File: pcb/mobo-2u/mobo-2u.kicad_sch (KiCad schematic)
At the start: 66 parts, among them J1 SWD_10, J2 PEEL_MOTOR, J3 DRIVE_MOTOR, J4 SW1, J5 SPRING_FINGERS, J6 SW2, J7 SW1, J8 USART1, J9 SWD_10, U1 STM32F031C6Tx, U2 STM32F031K6Ux, U4 AP1117-33, U5 MC34063AD, U6 MAX3078E, U7 DRV8837, U8 DRV8837, Y1 8MHz

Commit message: mega push, lots of cad updates, new pcb form factor and schematic rework
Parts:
- removed C12: 100uF, Capacitor_SMD:C_Elec_6.3x7.7, symbol Device:C_Polarized_Small
- removed C13, C9: 10u, Capacitor_SMD:C_0805_2012Metric, symbol Device:C_Small
- removed C14: 470pF, Capacitor_SMD:C_0805_2012Metric, symbol Device:C_Small
- removed C16: 470uF, Capacitor_SMD:C_Elec_6.3x7.7, symbol Device:C_Polarized_Small
- removed D1: LED_RGBA, index:MHS110FRGBCT, symbol Device:LED_RGBA
- removed D3: LED_RGBA_ALT, LED_SMD:LED_LiteOn_LTST-C19HE1WT, symbol Device:LED_RGBA
- removed D6: 1N5819, Diode_SMD:D_SOD-123, symbol Diode:1N5819
- removed J4, J7: SW1, feeder:1TS003B-1400-3500A-CT, symbol Connector:Conn_01x04_Female
- removed J6: SW2, feeder:1TS003B-1400-3500A-CT, symbol Connector:Conn_01x04_Female
- removed L1: 220uH, Inductor_SMD:L_6.3x6.3_H3, symbol pspice:INDUCTOR
- removed R2, R3, R5: 470, Resistor_SMD:R_0805_2012Metric, symbol Device:R_Small
- removed U1: STM32F031C6Tx, Package_QFP:LQFP-48_7x7mm_P0.5mm, symbol MCU_ST_STM32F0:STM32F031C6Tx
- removed U2: STM32F031K6Ux, Package_DFN_QFN:QFN-32-1EP_5x5mm_P0.5mm_EP3.45x3.45mm, symbol MCU_ST_STM32F0:STM32F031K6Ux
- removed U4: AP1117-33, Package_TO_SOT_SMD:SOT-223-3_TabPin2, symbol Regulator_Linear:AP1117-33
- removed U5: MC34063AD, Package_SO:SOIC-8_3.9x4.9mm_P1.27mm, symbol Regulator_Switching:MC34063AD
- added C15, C21, C25, C26, C27, C28: 10u, Capacitor_SMD:C_0805_2012Metric, symbol Device:C_Small
- added C16: 1u, Capacitor_SMD:C_0805_2012Metric, symbol Device:C_Small
- added C22: 4.7n, Capacitor_SMD:C_0805_2012Metric, symbol Device:C_Small
- added C23: 47p, Capacitor_SMD:C_0805_2012Metric, symbol Device:C_Small
- added C24: 100n, Capacitor_SMD:C_0805_2012Metric, symbol Device:C_Small
- added C29: 0.1n, Capacitor_SMD:C_0805_2012Metric, symbol Device:C_Small
- added D4: B560C, Diode_SMD:D_SMC, symbol Device:D_Schottky
- added L2: 8.2uH, Inductor_SMD:L_Taiyo-Yuden_NR-50xx, symbol Device:L_Small
- added R10: 4.7k, Resistor_SMD:R_0805_2012Metric, symbol Device:R_Small
- added R11: 243k, Resistor_SMD:R_0805_2012Metric, symbol Device:R_Small
- added R12: 16.9k, Resistor_SMD:R_0805_2012Metric, symbol Device:R_Small
- added R18, R8: 10k, Resistor_SMD:R_0805_2012Metric, symbol Device:R_Small
- added R19: 820R, Resistor_SMD:R_0805_2012Metric, symbol Device:R_Small
- added SW3: BACK_BTN, feeder:SKTDLDE010, symbol feeder:SKTDLDE010
- added SW4: FWD_BTN, feeder:SKTDLDE010, symbol feeder:SKTDLDE010
- added SW5: RESET_BTN, feeder:SKTDLDE010, symbol feeder:SKTDLDE010
- added TP9: TP_24V, TestPoint:TestPoint_Pad_D2.0mm, symbol Connector:TestPoint
- added U2: MHS110FRGBCT, index:MHS110FRGBCT, symbol feeder:MHS110FRGBCT
- added U3: STM32F030C8Tx, Package_QFP:LQFP-48_7x7mm_P0.5mm, symbol MCU_ST_STM32F0:STM32F030C8Tx
- added U5: AP2210, Package_TO_SOT_SMD:SOT-23-5, symbol feeder:AP2210
- added U9: TPS54560BDDA, Package_SO:Texas_R-PDSO-G8_EP2.95x4.9mm_Mask2.4x3.1mm_ThermalVias, symbol Regulator_Switching:TPS54560BDDA
- R13: value 0.33R -> 470; JLCPCB (none) -> C17710; LCSC (none) -> C119076
- R6: value 5.6k -> 470; JLCPCB (none) -> C17710; LCSC (none) -> C119076
- R9: value 39k -> 470; JLCPCB (none) -> C17710; LCSC (none) -> C119076
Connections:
- net +10V: now also C16.1, C25.2, C26.2, C27.2, L2.2, R18.1, U5.1 (VIN), U5.3 (EN); no longer R9.2
- net +3V3: now also C28.1, SW5.1 (TERM1), U2.1 (ANODE), U3.1 (VDD), U3.24 (VDD), U3.48 (VDD), U3.9 (VDDA), U5.5 (VOUT)
- net +VDC: now also C15.1, C21.1, R8.1, TP9.1, U9.2 (VIN); no longer R13.1
- net 1WIRE: now also U3.29 (PA8)
- net BOOT0: now also SW5.2 (TERM2), U3.44 (BOOT0)
- net DE: now also U3.33 (PA12)
- net DRIVE1: now also U3.40 (PB4)
- net DRIVE2: now also U3.41 (PB5)
- net DRIVE_QUAD_A: now also U3.42 (PB6)
- net DRIVE_QUAD_B: now also U3.43 (PB7)
- net GND: now also C15.2, C16.2, C21.2, C22.2, C23.2, C25.1, C26.1, C27.1, C28.2, C29.2, D4.2 (A), R10.2, R11.2, R19.2, SW3.2 (TERM2), SW3.3 (MNT1), SW3.4 (MNT2), SW4.2 (TERM2), SW4.3 (MNT1), SW4.4 (MNT2), SW5.3 (MNT1), SW5.4 (MNT2), U3.23 (VSS), U3.47 (VSS), U3.8 (VSSA), U5.2 (GND), U9.7 (GND), U9.9 (GND); no longer R6.2
- net LED_B: now also R13.1, U3.14 (PA4)
- net LED_G: now also R9.1, U3.16 (PA6)
- net LED_R: now also R6.1, U3.17 (PA7)
- net MCU_RX: now also U3.31 (PA10)
- net MCU_TX: now also U3.30 (PA9)
- net MOTOR_ENABLE: now also U3.12 (PA2)
- net OSC_IN: now also U3.5 (PF0)
- net OSC_OUT: now also U3.6 (PF1)
- net PA0: now also U3.10 (PA0)
- net PA1: now also U3.11 (PA1)
- net PA3: now also U3.13 (PA3)
- net PEEL1: now also U3.39 (PB3)
- net PEEL2: now also U3.38 (PA15)
- net RESET: now also U3.7 (NRST)
- net SW1: now also SW3.1 (TERM1), U3.19 (PB1)
- net SW2: now also SW4.1 (TERM1), U3.18 (PB0)
- net SWCLK: now also U3.37 (PA14)
- net SWDIO: now also U3.34 (PA13)
- net ~{RE}: now also U3.32 (PA11)
- net at R13.2: now also U2.2 (BLUE)
- new net: R18.2, R19.1, U9.5 (FB)
- new net: C29.1, U5.4 (BYP/ADJ)
- new net: C24.2, D4.1 (K), L2.1, U9.8 (SW)
- new net: C23.1, R12.1, U9.6 (COMP)
- new net: C22.1, R12.2
- new net: R10.1, R8.2, U9.3 (EN)
- new net: C24.1, U9.1 (BOOT)
- new net: R6.2, U2.4 (RED)
- new net: R9.2, U2.3 (GREEN)
- new net: R11.1, U9.4 (RT/CLK)
- no-connect marks 8 -> 4
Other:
- note removed: "DNP"
- moved on the sheet: C1, C10, C11, C17, C18, C19, C2, C20, C3, C4, C5, C6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

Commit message: small tweaks
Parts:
- removed C16: 1u, Capacitor_SMD:C_0805_2012Metric, symbol Device:C_Small
- removed C28: 10u, Capacitor_SMD:C_0805_2012Metric, symbol Device:C_Small
- removed C29: 0.1n, Capacitor_SMD:C_0805_2012Metric, symbol Device:C_Small
- removed TP1: TP_3V3, TestPoint:TestPoint_Pad_D2.0mm, symbol Connector:TestPoint
- removed U5: AP2210, Package_TO_SOT_SMD:SOT-23-5, symbol feeder:AP2210
- added C30: 10uF, Capacitor_SMD:C_0805_2012Metric, symbol Device:C_Small
- added C31: 100nF, Capacitor_SMD:C_0805_2012Metric, symbol Device:C_Small
- added C32, C33: 22uF, Capacitor_SMD:C_0805_2012Metric, symbol Device:C_Small
- added D1: SMF28A, Diode_SMD:D_SMF, symbol Diode:SMF28A
- added L1: 3.9uH, Inductor_SMD:L_Changjiang_FNR3015S, symbol Device:L_Small
- added TP10: TP_3V3, TestPoint:TestPoint_Pad_D2.0mm, symbol Connector:TestPoint
- added U1: AP63203WU, Package_TO_SOT_SMD:TSOT-23-6, symbol Regulator_Switching:AP63203WU
- J1, J9: now not fitted
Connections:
- net +10V: now also C30.1, U1.2 (EN), U1.3 (IN)
- net +3V3: now also C32.1, C33.1, L1.2, TP10.1, U1.1 (FB)
- net +VDC: now also D1.1 (A1)
- net GND: now also C30.2, C32.2, C33.2, D1.2 (A2), U1.4 (GND)
- new net: C31.2, L1.1, U1.5 (SW)
- new net: C31.1, U1.6 (BST)

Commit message: rev00b1 pcb, working cad. about to try to test parametric for 16mm
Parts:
- removed J9: SWD_10, Connector_PinHeader_1.27mm:PinHeader_2x05_P1.27mm_Vertical_SMD, symbol Connector:Conn_ARM_JTAG_SWD_10
- added D3, D5, D6: PESD3V3S1UL, Diode_SMD:D_SOD-882, symbol Diode:PESD3V3S1UL
- added TP1: TP_RESET, TestPoint:TestPoint_Pad_D2.0mm, symbol Connector:TestPoint
- added TP11: TP_SWCLK, TestPoint:TestPoint_Pad_D2.0mm, symbol Connector:TestPoint
- added TP12: TP_SWDIO, TestPoint:TestPoint_Pad_D2.0mm, symbol Connector:TestPoint
- added U4: ~, Package_TO_SOT_SMD:SOT-23, symbol feeder:DRV5053VAQDBZR
- J2: footprint Connector_Molex:Molex_PicoBlade_53261-0271_1x02-1MP_P1.25mm_Horizontal -> Connector_Molex:Molex_PicoBlade_53398-0271_1x02-1MP_P1.25mm_Vertical
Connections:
- net PA0 is gone; now on net ~{RE}: U3.10 (PA0)
- net PA1 is gone; now on net DE: U3.11 (PA1)
- net +3V3: now also D6.1 (K), U4.1 (VCC)
- net DE: no longer U3.33 (PA12)
- net DRIVE1: now also U3.16 (PA6); no longer U3.40 (PB4)
- net DRIVE2: now also U3.17 (PA7); no longer U3.41 (PB5)
- net DRIVE_QUAD_A: now also U3.14 (PA4); no longer U3.42 (PB6)
- net DRIVE_QUAD_B: now also U3.15 (PA5); no longer U3.43 (PB7)
- net GND: now also D3.2 (A), D5.2 (A), D6.2 (A), U4.3 (GND)
- net LED_B: now also U3.40 (PB4); no longer U3.14 (PA4)
- net LED_G: now also U3.19 (PB1); no longer U3.16 (PA6)
- net LED_R: now also U3.18 (PB0); no longer U3.17 (PA7)
- net MCU_RX: now also D3.1 (K); no longer U6.1 (RO)
- net MCU_TX: now also D5.1 (K); no longer U6.4 (DI)
- net MOTOR_ENABLE: now also U3.43 (PB7); no longer U3.12 (PA2)
- net OSC_IN: now also U3.3 (PC14); no longer U3.5 (PF0)
- net OSC_OUT: now also U3.4 (PC15); no longer U3.6 (PF1)
- net PEEL1: now also U3.45 (PB8); no longer U3.39 (PB3)
- net PEEL2: now also U3.46 (PB9); no longer U3.38 (PA15)
- net RESET: now also TP1.1
- net SW1: now also U3.42 (PB6); no longer U3.19 (PB1)
- net SW2: now also U3.41 (PB5); no longer U3.18 (PB0)
- net SWCLK: now also TP11.1
- net SWDIO: now also TP12.1
- net ~{RE}: no longer U3.32 (PA11)
- net FILM_TENSION: now reaches U3.20 (PB2)
- net FILM_TENSION: now also U4.2 (OUT)
- net PA3 renamed PHOTON_RX
- net PHOTON_RX: now also U6.1 (RO)
- new net PHOTON_TX: U3.12 (PA2), U6.4 (DI)
- no-connect marks 4 -> 2
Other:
- moved on the sheet: C6, D9, J5, R14, TP9

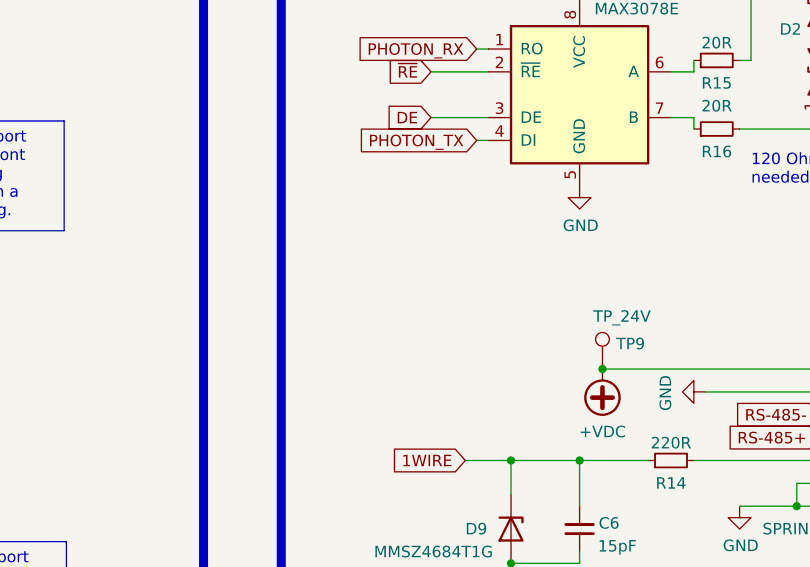
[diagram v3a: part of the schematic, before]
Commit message: few more geometry tweaks, makes peel gear disengage fully
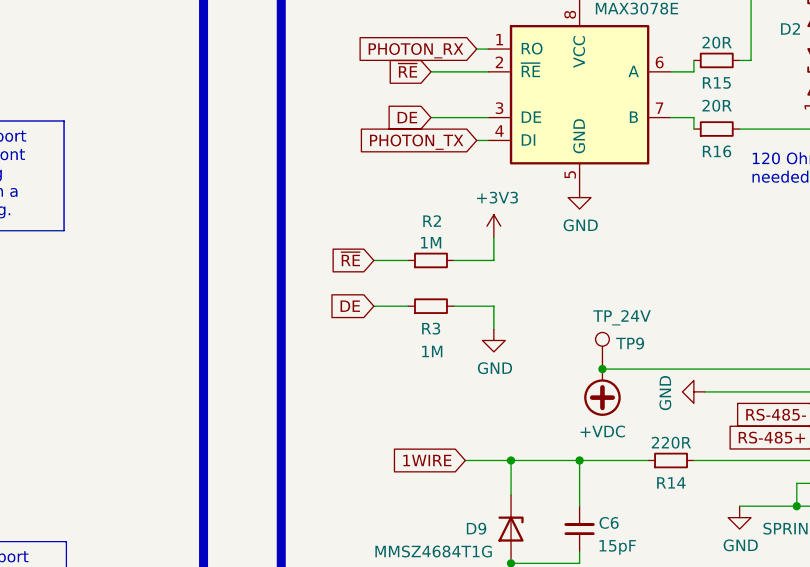
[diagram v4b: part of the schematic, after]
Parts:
- added R2, R3: 1M, Resistor_SMD:R_0805_2012Metric, symbol Device:R_Small
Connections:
- net +3V3: now also R2.2
- net DE: now also R3.1
- net GND: now also R3.2
- net ~{RE}: now also R2.1

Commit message: tweaks to pcb, adds supportless features to frame, id fid slot
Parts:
- removed U4: ~, Package_TO_SOT_SMD:SOT-23, symbol feeder:DRV5053VAQDBZR
- added TP13: TP_RESET, TestPoint:TestPoint_Pad_D2.0mm, symbol Connector:TestPoint
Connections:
- net GND: now also TP13.1
- net OSC_IN: now also U3.5 (PF0); no longer U3.3 (PC14)
- net OSC_OUT: now also U3.6 (PF1); no longer U3.4 (PC15)
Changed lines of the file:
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@@
 	(wire
 		(pts
-			(xy 428.625 116.205) (xy 430.53 116.205)
-		)
-		(stroke
-			(width 0)
-			(type default)
-		)
-	)
-	(wire
-		(pts
 			(xy 378.46 93.345) (xy 385.445 93.345)
 		)
@@
 	(wire
 		(pts
-			(xy 428.625 125.095) (xy 430.53 125.095)
+			(xy 137.795 34.29) (xy 137.795 34.925)
 		)
 		(stroke
@@
 	(wire
 		(pts
-			(xy 448.31 120.015) (xy 450.215 120.015)
-		)
-		(stroke
-			(width 0)
-			(type default)
-		)
-	)
-	(wire
-		(pts
 			(xy 342.265 89.535) (xy 342.265 92.075)
 		)
@@
 	(wire
 		(pts
+			(xy 135.89 34.29) (xy 137.795 34.29)
+		)
+		(stroke
+			(width 0)
+			(type default)
+		)
+	)
+	(wire
+		(pts
 			(xy 76.835 200.025) (xy 85.725 200.025)
 		)
@@
 	(global_label "OSC_OUT"
 		(shape input)
-		(at 47.625 74.93 180)
+		(at 47.625 59.69 180)
 		(fields_autoplaced yes)
 		(effects
@@
 		)
 		(property "Intersheetrefs" "${INTERSHEET_REFS}"
-			(at 36.8946 74.8506 0)
+			(at 36.8946 59.6106 0)
 			(effects
 				(font
@@
 	(global_label "OSC_IN"
 		(shape input)
-		(at 47.625 72.39 180)
+		(at 47.625 57.15 180)
 		(fields_autoplaced yes)
 		(effects
@@
 		)
 		(property "Intersheetrefs" "${INTERSHEET_REFS}"
-			(at 38.5879 72.4694 0)
+			(at 38.5879 57.2294 0)
 			(effects
 				(font
@@
 		)
 	)
-	(global_label "FILM_TENSION"
-		(shape input)
-		(at 450.215 120.015 0)
-		(fields_autoplaced yes)
-		(effects
-			(font
-				(size 1.27 1.27)
-			)
-			(justify left)
-		)
-		(property "Intersheetrefs" "${INTERSHEET_REFS}"
-			(at 464.7137 120.015 0)
-			(effects
-				(font
-					(size 1.27 1.27)
-				)
-				(justify left)
-				(hide yes)
-			)
-		)
-	)
 	(global_label "RS-485-"
 		(shape input)
@@
 	)
 	(symbol
-		(lib_id "feeder:DRV5053VAQDBZR")
-		(at 439.42 120.015 0)
-		(unit 1)
-		(exclude_from_sim no)
-		(in_bom yes)
-		(on_board yes)
-		(dnp no)
-		(fields_autoplaced yes)
-		(property "Reference" "U4"
-			(at 439.42 110.627 0)
-			(effects
-				(font
-					(size 1.27 1.27)
-				)
-			)
-		)
-		(property "Value" "~"
-			(at 439.42 112.0775 0)
-			(effects
-				(font
-					(size 1.27 1.27)
-				)
-			)
-		)
-		(property "Footprint" "Package_TO_SOT_SMD:SOT-23"
-			(at 438.912 129.921 0)
-			(effects
-				(font
-					(size 1.27 1.27)
-				)
-				(hide yes)
-			)
-		)
-		(property "Datasheet" "https://www.ti.com/lit/ds/symlink/drv5053.pdf"
-			(at 439.166 134.493 0)
-			(effects
-				(font
-					(size 1.27 1.27)
-				)
-				(hide yes)
-			)
-		)
-		(property "Description" "Analog-Bipolar Hall Effect Sensor"
-			(at 439.42 132.207 0)
-			(effects
-				(font
-					(size 1.27 1.27)
-				)
-				(hide yes)
-			)
-		)
-		(pin "1"
-		)
-		(pin "3"
-		)
-		(pin "2"
-		)
-		(instances
-			(project ""
-				(path "/e502d1d5-04b0-4d4b-b5c3-8c52d09668e7"
-					(reference "U4")
-					(unit 1)
-				)
-			)
-		)
-	)
-	(symbol
 		(lib_id "Device:R_Small")
 		(at 332.105 81.915 180)
@@
 	(symbol
 		(lib_id "power:GND")
-		(at 428.625 125.095 0)
-		(unit 1)
-		(exclude_from_sim no)
-		(in_bom yes)
-		(on_board yes)
-		(dnp no)
-		(property "Reference" "#PWR0122"
-			(at 428.625 131.445 0)
-			(effects
-				(font
-					(size 1.27 1.27)
-				)
-				(hide yes)
-			)
-		)
-		(property "Value" "GND"
-			(at 428.752 129.4892 0)
-			(effects
-				(font
-					(size 1.27 1.27)
-				)
-			)
-		)
-		(property "Footprint" ""
-			(at 428.625 125.095 0)
-			(effects
-				(font
-					(size 1.27 1.27)
-				)
-				(hide yes)
-			)
-		)
-		(property "Datasheet" ""
-			(at 428.625 125.095 0)
-			(effects
-				(font
-					(size 1.27 1.27)
-				)
-				(hide yes)
-			)
-		)
-		(property "Description" ""
-			(at 428.625 125.095 0)
-			(effects
-				(font
-					(size 1.27 1.27)
-				)
-				(hide yes)
-			)
-		)
-		(pin "1"
-		)
-		(instances
-			(project "mobo-2u"
-				(path "/e502d1d5-04b0-4d4b-b5c3-8c52d09668e7"
-					(reference "#PWR0122")
-					(unit 1)
-				)
-			)
-		)
-	)
-	(symbol
-		(lib_id "power:+3V3")
-		(at 428.625 116.205 0)
-		(unit 1)
-		(exclude_from_sim no)
-		(in_bom yes)
-		(on_board yes)
-		(dnp no)
-		(property "Reference" "#PWR08"
-			(at 428.625 120.015 0)
-			(effects
-				(font
-					(size 1.27 1.27)
-				)
-				(hide yes)
-			)
-		)
-		(property "Value" "+3V3"
-			(at 429.006 111.8108 0)
-			(effects
-				(font
-					(size 1.27 1.27)
-				)
-			)
-		)
-		(property "Footprint" ""
-			(at 428.625 116.205 0)
-			(effects
-				(font
-					(size 1.27 1.27)
-				)
-				(hide yes)
-			)
-		)
-		(property "Datasheet" ""
-			(at 428.625 116.205 0)
-			(effects
-				(font
-					(size 1.27 1.27)
-				)
-				(hide yes)
-			)
-		)
-		(property "Description" ""
-			(at 428.625 116.205 0)
-			(effects
-				(font
-					(size 1.27 1.27)
-				)
-				(hide yes)
-			)
-		)
-		(pin "1"
-		)
-		(instances
-			(project "mobo-2u"
-				(path "/e502d1d5-04b0-4d4b-b5c3-8c52d09668e7"
-					(reference "#PWR08")
-					(unit 1)
-				)
-			)
-		)
-	)
-	(symbol
-		(lib_id "power:GND")
 		(at 281.305 114.3 0)
 		(unit 1)
@@
 	)
 	(symbol
+		(lib_id "power:GND")
+		(at 137.795 34.925 0)
+		(unit 1)
+		(exclude_from_sim no)
+		(in_bom yes)
+		(on_board yes)
+		(dnp no)
+		(property "Reference" "#PWR012"
+			(at 137.795 41.275 0)
+			(effects
+				(font
+					(size 1.27 1.27)
+				)
+				(hide yes)
+			)
+		)
+		(property "Value" "GND"
+			(at 137.922 39.3192 0)
+			(effects
+				(font
+					(size 1.27 1.27)
+				)
+			)
+		)
+		(property "Footprint" ""
+			(at 137.795 34.925 0)
+			(effects
+				(font
+					(size 1.27 1.27)
+				)
+				(hide yes)
+			)
+		)
+		(property "Datasheet" ""
+			(at 137.795 34.925 0)
+			(effects
+				(font
+					(size 1.27 1.27)
+				)
+				(hide yes)
+			)
+		)
+		(property "Description" ""
+			(at 137.795 34.925 0)
+			(effects
+				(font
+					(size 1.27 1.27)
+				)
+				(hide yes)
+			)
+		)
+		(pin "1"
+		)
+		(instances
+			(project "mobo-2u"
+				(path "/e502d1d5-04b0-4d4b-b5c3-8c52d09668e7"
+					(reference "#PWR012")
+					(unit 1)
+				)
+			)
+		)
+	)
+	(symbol
 		(lib_id "Device:C_Small")
 		(at 124.46 126.365 180)
@@
 					(unit 1)
 				)
+			)
+		)
+	)
+	(symbol
+		(lib_id "Connector:TestPoint")
+		(at 135.89 34.29 90)
+		(unit 1)
+		(exclude_from_sim no)
+		(in_bom yes)
+		(on_board yes)
+		(dnp no)
+		(property "Reference" "TP13"
+			(at 131.6795 32.893 0)
+			(effects
+				(font
+					(size 1.27 1.27)
+				)
+				(justify left)
+			)
+		)
+		(property "Value" "TP_RESET"
+			(at 134.62 33.02 0)
+			(effects
+				(font
+					(size 1.27 1.27)
+				)
+				(justify left)
+			)
+		)
+		(property "Footprint" "TestPoint:TestPoint_Pad_D2.0mm"
+			(at 135.89 29.21 0)
+			(effects
+				(font
+					(size 1.27 1.27)
+				)
+				(hide yes)
+			)
+		)
+		(property "Datasheet" "~"
+			(at 135.89 29.21 0)
+			(effects
+				(font
+					(size 1.27 1.27)
+				)
+				(hide yes)
+			)
+		)
+		(property "Description" ""
+			(at 135.89 34.29 0)
+			(effects
+				(font
+					(size 1.27 1.27)
+				)
+				(hide yes)
+			)
+		)
+		(pin "1"
+		)
+		(instances
+			(project "mobo-2u"
+				(path "/e502d1d5-04b0-4d4b-b5c3-8c52d09668e7"
+					(reference "TP13")
+					(unit 1)
+				)

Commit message: this commit reflects rev00b2 pcb
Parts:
- removed C15, C21, C25, C26, C27: 10u, Capacitor_SMD:C_0805_2012Metric, symbol Device:C_Small
- removed C22: 4.7n, Capacitor_SMD:C_0805_2012Metric, symbol Device:C_Small
- removed C23: 47p, Capacitor_SMD:C_0805_2012Metric, symbol Device:C_Small
- removed C24: 100n, Capacitor_SMD:C_0805_2012Metric, symbol Device:C_Small
- removed D1: SMF28A, Diode_SMD:D_SMF, symbol Diode:SMF28A
- removed D4: B560C, Diode_SMD:D_SMC, symbol Device:D_Schottky
- removed L2: 8.2uH, Inductor_SMD:L_Taiyo-Yuden_NR-50xx, symbol Device:L_Small
- removed R10: 4.7k, Resistor_SMD:R_0805_2012Metric, symbol Device:R_Small
- removed R11: 243k, Resistor_SMD:R_0805_2012Metric, symbol Device:R_Small
- removed R12: 16.9k, Resistor_SMD:R_0805_2012Metric, symbol Device:R_Small
- removed R18, R8: 10k, Resistor_SMD:R_0805_2012Metric, symbol Device:R_Small
- removed R19: 820R, Resistor_SMD:R_0805_2012Metric, symbol Device:R_Small
- removed TP2: TP_10V, TestPoint:TestPoint_Pad_D2.0mm, symbol Connector:TestPoint
- removed U9: TPS54560BDDA, Package_SO:Texas_R-PDSO-G8_EP2.95x4.9mm_Mask2.4x3.1mm_ThermalVias, symbol Regulator_Switching:TPS54560BDDA
- added C12: 100nF, Capacitor_SMD:C_0805_2012Metric, symbol Device:C_Small
- added C13: 56pF, Capacitor_SMD:C_0805_2012Metric, symbol Device:C_Small
- added C14, C16: 22uF, Capacitor_SMD:C_0805_2012Metric, symbol Device:C_Small
- added C9: 10uF, Capacitor_SMD:C_0805_2012Metric, symbol Device:C_Small
- added D7: SMF28A, Diode_SMD:D_SMF, symbol Diode:SMF28A
- added L3: 10uH, Inductor_SMD:L_Changjiang_FNR3015S, symbol Device:L_Small
- added R20: 18k, Resistor_SMD:R_0805_2012Metric, symbol Device:R_Small
- added R5: 218k, Resistor_SMD:R_0805_2012Metric, symbol Device:R_Small
- added TP14: TP_10V, TestPoint:TestPoint_Pad_D2.0mm, symbol Connector:TestPoint
- added U4: AP63200WU, Package_TO_SOT_SMD:TSOT-23-6, symbol Regulator_Switching:AP63200WU
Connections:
- net +10V: now also C13.2, C14.2, C16.2, L3.2, R5.2, TP14.1
- net +VDC: now also C9.1, D7.1 (A1), U4.2 (EN), U4.3 (IN)
- net GND: now also C14.1, C16.1, C9.2, D7.2 (A2), R20.1, U4.4 (GND)
- new net: C13.1, R20.2, R5.1, U4.1 (FB)
- new net: C12.2, L3.1, U4.5 (SW)
- new net: C12.1, U4.6 (BST)
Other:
- note removed: "At least 24V tolerant for VDC"

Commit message: updates stickers, tweaks
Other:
- moved on the sheet: C12, C13, C14, C16, C30, C31, C32, C33, C9, D7, L1, L3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
